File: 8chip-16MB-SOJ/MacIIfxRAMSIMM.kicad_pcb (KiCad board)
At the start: 4 copper layers, 97.8 x 25.4 mm, 27 parts, among them J1 IIfxRAM, U1 KM41C16000, U2 KM41C16000, U3 KM41C16000, U4 KM41C16000, U5 KM41C16000, U6 KM41C16000, U7 KM41C16000, U8 KM41C16000

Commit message: 8chip SOJ SIMM done?
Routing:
- net GND: vias 159 -> 161
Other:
- board text added: "4407A"
- board text removed: "4406A"
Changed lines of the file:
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@@
     (thickness 1.6)
     (drawings 24)
-    (tracks 1291)
+    (tracks 1293)
     (zones 0)
     (modules 27)
@@
     (effects (font (size 1.5 1.5) (thickness 0.3)) (justify right mirror))
   )
-  (gr_text 4406A (at 146.452286 116.967) (layer B.SilkS)
+  (gr_text 4407A (at 146.452286 116.967) (layer B.SilkS)
     (effects (font (size 1.5 1.5) (thickness 0.3)) (justify left mirror))
   )
@@
   (via (at 163.83 103.251) (size 0.508) (drill 0.2) (layers F.Cu B.Cu) (net 6))
   (via (at 158.75 103.251) (size 0.508) (drill 0.2) (layers F.Cu B.Cu) (net 6))
+  (via (at 120.7135 111.0615) (size 0.5) (drill 0.2) (layers F.Cu B.Cu) (net 6))
+  (via (at 120.5865 112.3315) (size 0.5) (drill 0.2) (layers F.Cu B.Cu) (net 6))
   (via (at 124.841 108.204) (size 0.5) (drill 0.2) (layers F.Cu B.Cu) (net 7))
   (segment (start 124.841 108.204) (end 122.936 108.204) (width 0.15) (layer F.Cu) (net 7))

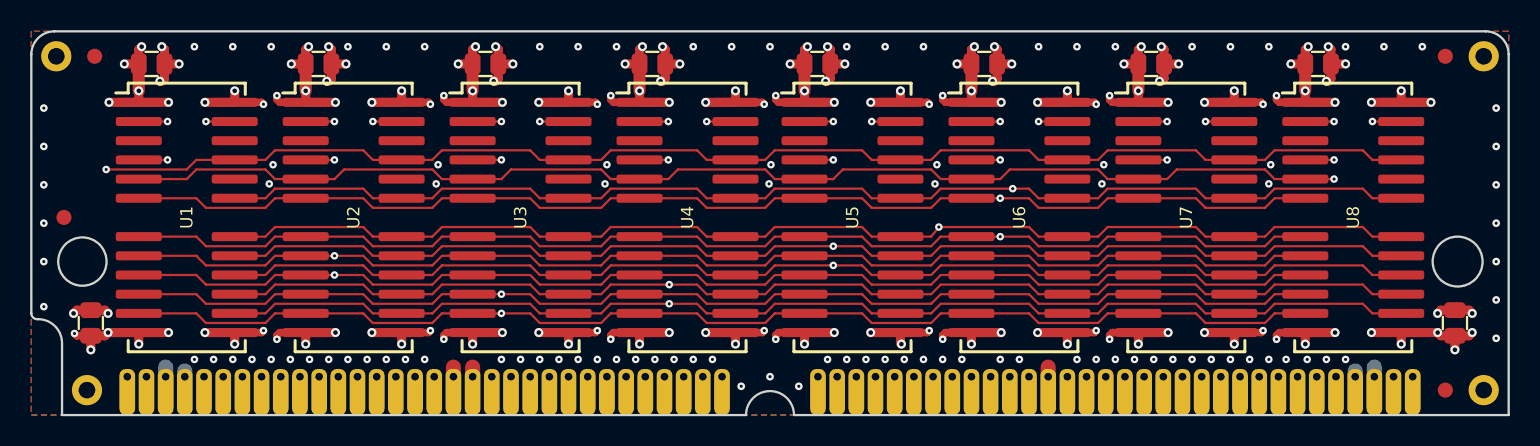
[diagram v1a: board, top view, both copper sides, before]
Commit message: Migrate to KiCAD 6
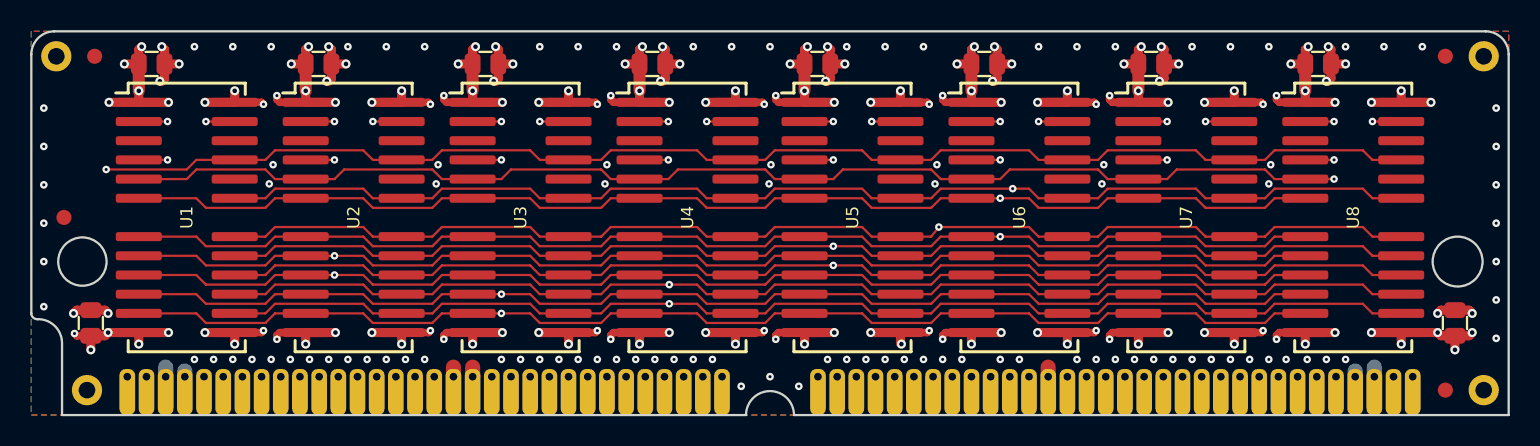
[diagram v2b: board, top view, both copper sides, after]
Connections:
- net /~CAS~ renamed /~{CAS}
- net /~Q~B renamed /~{Q}B
- net /~RAS~ renamed /~{RAS}
- net /~WWP~ renamed /~{WWP}
- net /~W~0 renamed /~{W}0
- net /~W~1 renamed /~{W}1
- net /~W~2 renamed /~{W}2
- net /~W~3 renamed /~{W}3
- net /~W~4 renamed /~{W}4
- net /~W~5 renamed /~{W}5
- net /~W~6 renamed /~{W}6
- net /~W~7 renamed /~{W}7
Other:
- net class Default removed
